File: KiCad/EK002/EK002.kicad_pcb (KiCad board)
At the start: 2 copper layers, 132 x 100 mm, 83 parts, among them J1 BATT, J2 XKB_PJ-342B, SW1 D2FC, SW10 D2FC, SW11 D2FC, SW12 D2FC, SW13 D2FC, SW14 D2FC, SW15 D2FC, SW16 D2FC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

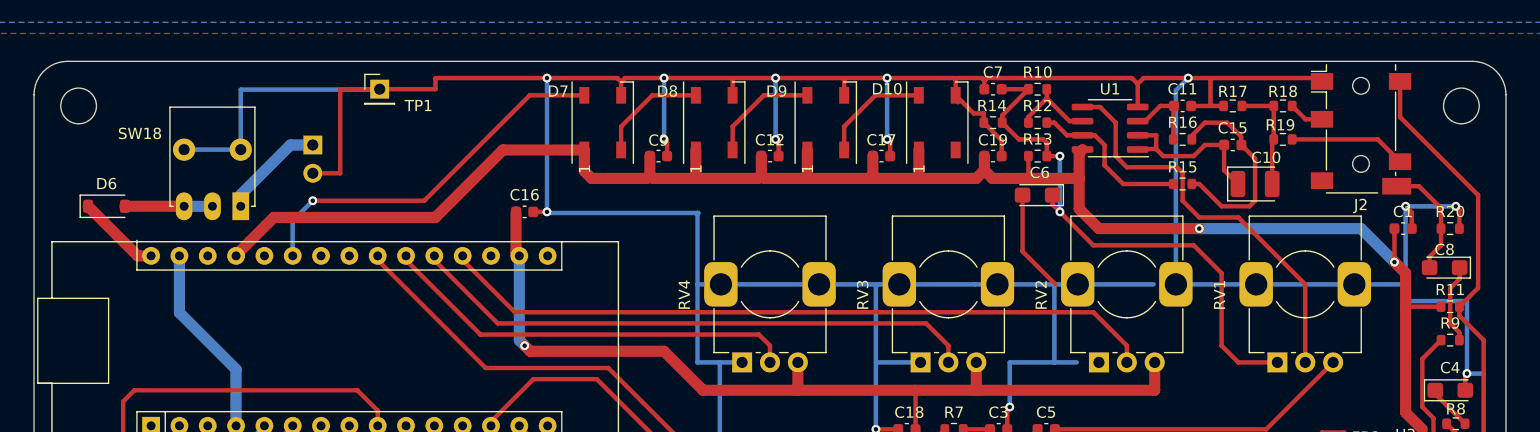
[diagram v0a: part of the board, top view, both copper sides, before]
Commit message: update 3d models
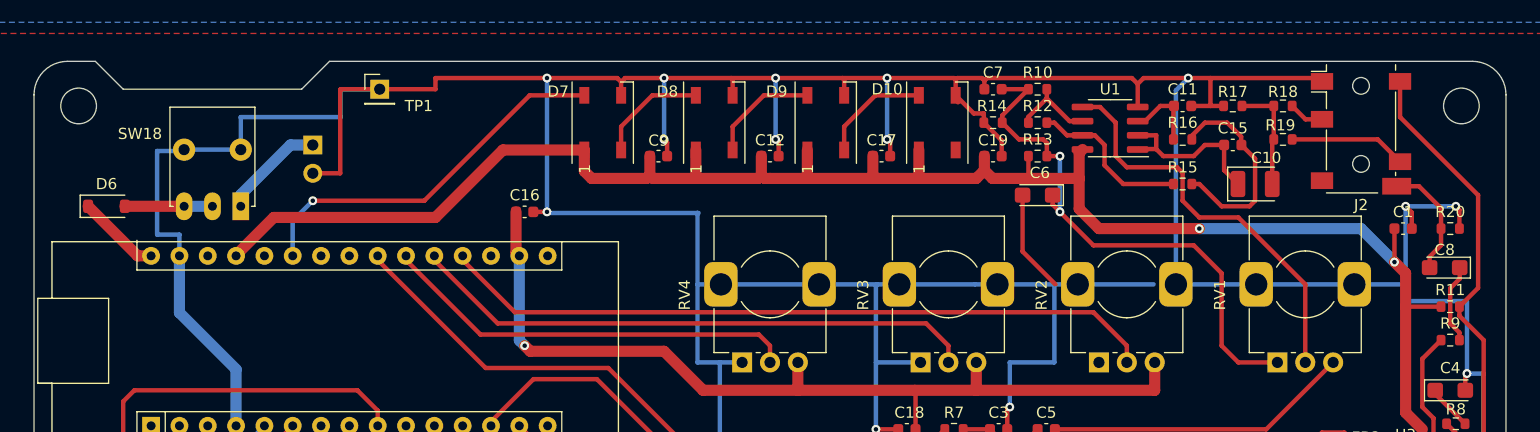
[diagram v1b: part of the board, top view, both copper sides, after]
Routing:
- net GND: track 518.8 -> 530.7 mm
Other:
- outline, holes or cut-outs redrawn
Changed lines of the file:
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@@
       (sketchpadsonfab false)
       (subtractmaskfromsilk false)
-      (outputformat 1)
+      (outputformat 4)
       (mirror false)
-      (drillshape 1)
+      (drillshape 0)
       (scaleselection 1)
       (outputdirectory "Gerber/")
@@
   (gr_line (start 182.4 149.78) (end 122.4 149.78)
     (stroke (width 0.1) (type solid)) (layer "Edge.Cuts"))
+  (gr_line (start 94.4 52.28) (end 110.4 52.28)
+    (stroke (width 0.1) (type default)) (layer "Edge.Cuts"))
+  (gr_line (start 94.4 52.28) (end 91.9 49.78)
+    (stroke (width 0.1) (type default)) (layer "Edge.Cuts"))
+  (gr_line (start 91.9 49.78) (end 89.4 49.78)
+    (stroke (width 0.1) (type default)) (layer "Edge.Cuts"))
   (gr_arc (start 215.4 49.78) (mid 217.52132 50.65868) (end 218.4 52.78)
     (stroke (width 0.1) (type solid)) (layer "Edge.Cuts"))
   (gr_line (start 86.4 114.78) (end 122.4 149.78)
     (stroke (width 0.1) (type default)) (layer "Edge.Cuts"))
+  (gr_line (start 110.4 52.28) (end 112.9 49.78)
+    (stroke (width 0.1) (type default)) (layer "Edge.Cuts"))
   (gr_line (start 218.4 52.78) (end 218.4 114.78)
     (stroke (width 0.1) (type solid)) (layer "Edge.Cuts"))
-  (gr_line (start 89.4 49.78) (end 215.4 49.78)
+  (gr_line (start 112.9 49.78) (end 215.4 49.78)
     (stroke (width 0.1) (type solid)) (layer "Edge.Cuts"))
   (gr_line (start 152.4 181.28) (end 152.4 24.78)
     (stroke (width 0.2) (type dash_dot)) (layer "F.Fab"))
-  (gr_text locked "EK-002" (at 147.4 95.78) (layer "F.SilkS")
+  (gr_text locked "EK-002 R2.0.1" (at 147.4 95.78) (layer "F.SilkS")
     (effects (font (size 1.5 1.5) (thickness 0.3)))
   )
@@
   (segment (start 104.94 57.7) (end 99.86 57.7) (width 0.4) (layer "B.Cu") (net 2))
   (segment (start 178 69.78) (end 186.8 69.78) (width 0.4) (layer "B.Cu") (net 2))
+  (segment (start 113.9 54.78) (end 113.9 52.32) (width 0.4) (layer "B.Cu") (net 2))
   (segment (start 147.9 76.78) (end 145.9 76.78) (width 0.4) (layer "B.Cu") (net 2))
-  (segment (start 117.36 52.32) (end 117.4 52.28) (width 0.4) (layer "B.Cu") (net 2))
+  (segment (start 99.44 65.32) (end 97.44 65.32) (width 0.4) (layer "B.Cu") (net 2))
   (segment (start 177.9 76.78) (end 177.9 69.88) (width 0.4) (layer "B.Cu") (net 2))
   (segment (start 104.9 90.28) (end 104.9 96.78) (width 0.4) (layer "B.Cu") (net 2))
@@
   (segment (start 146 63.38) (end 145.9 63.38) (width 0.4) (layer "B.Cu") (net 2))
   (segment (start 173.9 76.78) (end 177.9 76.78) (width 0.4) (layer "B.Cu") (net 2))
+  (segment (start 104.94 57.7) (end 104.94 54.78) (width 0.4) (layer "B.Cu") (net 2))
   (segment (start 173.9 80.78) (end 173.9 76.78) (width 0.4) (layer "B.Cu") (net 2))
   (segment (start 165.9 76.78) (end 161.9 76.78) (width 0.4) (layer "B.Cu") (net 2))
   (segment (start 132.4 88.28) (end 139.4 88.28) (width 0.4) (layer "B.Cu") (net 2))
-  (segment (start 104.94 57.7) (end 104.94 52.32) (width 0.4) (layer "B.Cu") (net 2))
   (segment (start 132.5 63.38) (end 132.4 63.28) (width 0.4) (layer "B.Cu") (net 2))
   (segment (start 104.9 96.78) (end 109.4 96.78) (width 0.4) (layer "B.Cu") (net 2))
@@
   (segment (start 161.9 69.88) (end 162 69.78) (width 0.4) (layer "B.Cu") (net 2))
   (segment (start 188.8 52.38) (end 189.9 51.28) (width 0.4) (layer "B.Cu") (net 2))
+  (segment (start 117.36 52.32) (end 117.4 52.28) (width 0.4) (layer "B.Cu") (net 2))
   (segment (start 209.4 62.78) (end 209.4 69.78) (width 0.4) (layer "B.Cu") (net 2))
   (segment (start 188.8 69.78) (end 188.8 52.38) (width 0.4) (layer "B.Cu") (net 2))
   (segment (start 209.4 69.78) (end 209.4 71.28) (width 0.4) (layer "B.Cu") (net 2))
   (segment (start 216.4 91.28) (end 216.4 77.78) (width 0.4) (layer "B.Cu") (net 2))
+  (segment (start 99.74 57.82) (end 99.86 57.7) (width 0.4) (layer "B.Cu") (net 2))
   (segment (start 216.4 77.78) (end 214.9 77.78) (width 0.4) (layer "B.Cu") (net 2))
+  (segment (start 97.44 57.82) (end 99.74 57.82) (width 0.4) (layer "B.Cu") (net 2))
   (segment (start 161.9 76.78) (end 161.9 69.88) (width 0.4) (layer "B.Cu") (net 2))
   (segment (start 99.44 72.32) (end 104.52 77.4) (width 1) (layer "B.Cu") (net 2))
@@
   (segment (start 202.4 91.28) (end 202.4 86.78) (width 0.4) (layer "B.Cu") (net 2))
   (segment (start 145.9 76.78) (end 145.9 69.78) (width 0.4) (layer "B.Cu") (net 2))
-  (segment (start 179.9 76.78) (end 177.9 76.78) (width 0.4) (layer "B.Cu") (net 2))
+  (segment (start 99.44 67.225) (end 99.44 65.32) (width 0.4) (layer "B.Cu") (net 2))
   (segment (start 161.9 82.78) (end 161.9 76.78) (width 0.4) (layer "B.Cu") (net 2))
   (segment (start 139.4 86.28) (end 139.4 88.28) (width 0.4) (layer "B.Cu") (net 2))
   (segment (start 213.9 62.78) (end 209.4 62.78) (width 0.4) (layer "B.Cu") (net 2))
-  (segment (start 104.94 52.32) (end 117.36 52.32) (width 0.4) (layer "B.Cu") (net 2))
+  (segment (start 97.44 65.32) (end 97.44 57.82) (width 0.4) (layer "B.Cu") (net 2))
+  (segment (start 113.9 52.32) (end 117.36 52.32) (width 0.4) (layer "B.Cu") (net 2))
+  (segment (start 104.94 54.78) (end 113.9 54.78) (width 0.4) (layer "B.Cu") (net 2))
   (segment (start 214.9 71.28) (end 209.4 71.28) (width 0.4) (layer "B.Cu") (net 2))
   (segment (start 170.8 69.78) (end 178 69.78) (width 0.4) (layer "B.Cu") (net 2))

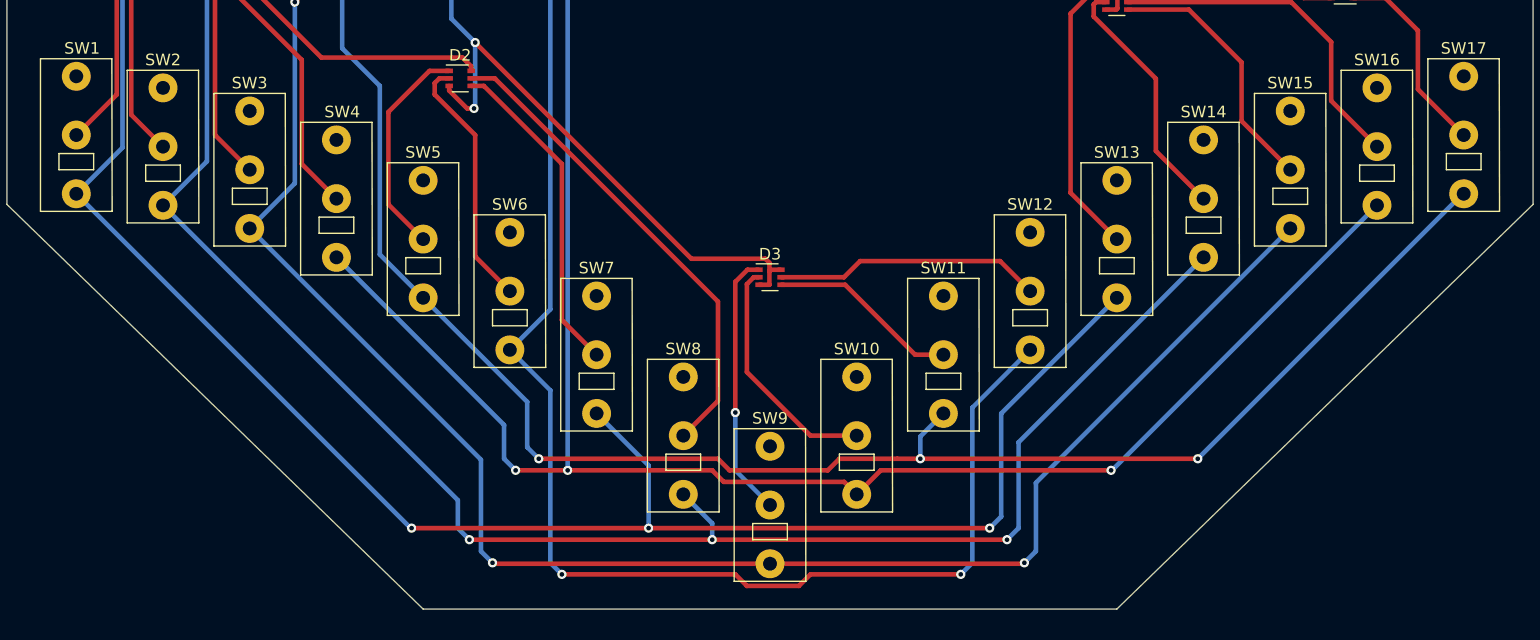
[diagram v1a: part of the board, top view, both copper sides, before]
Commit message: update 3d model / software
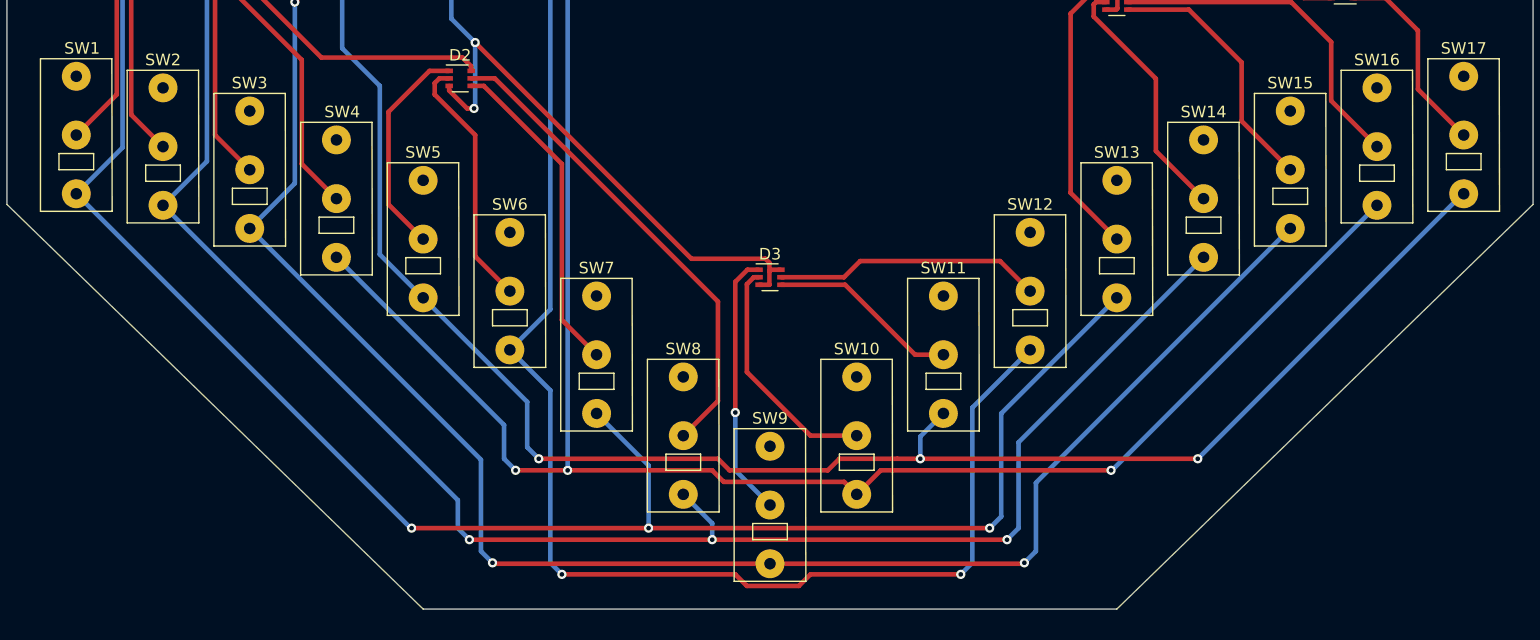
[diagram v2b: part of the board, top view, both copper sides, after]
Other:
- board text added: "+"
- board text added: "-"
- board text added: "BATT"
- board text added: "SP"
